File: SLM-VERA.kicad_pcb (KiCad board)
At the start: 2 copper layers, 28.4 x 47.9 mm, 25 parts, among them J1 FH35C-45S-0.3SHW(50), J2 FH35C-45S-0.3SHW(50), U1 FODM217D, U2 FODM217D, U3 FODM217D, U4 ESP32-DevKitC

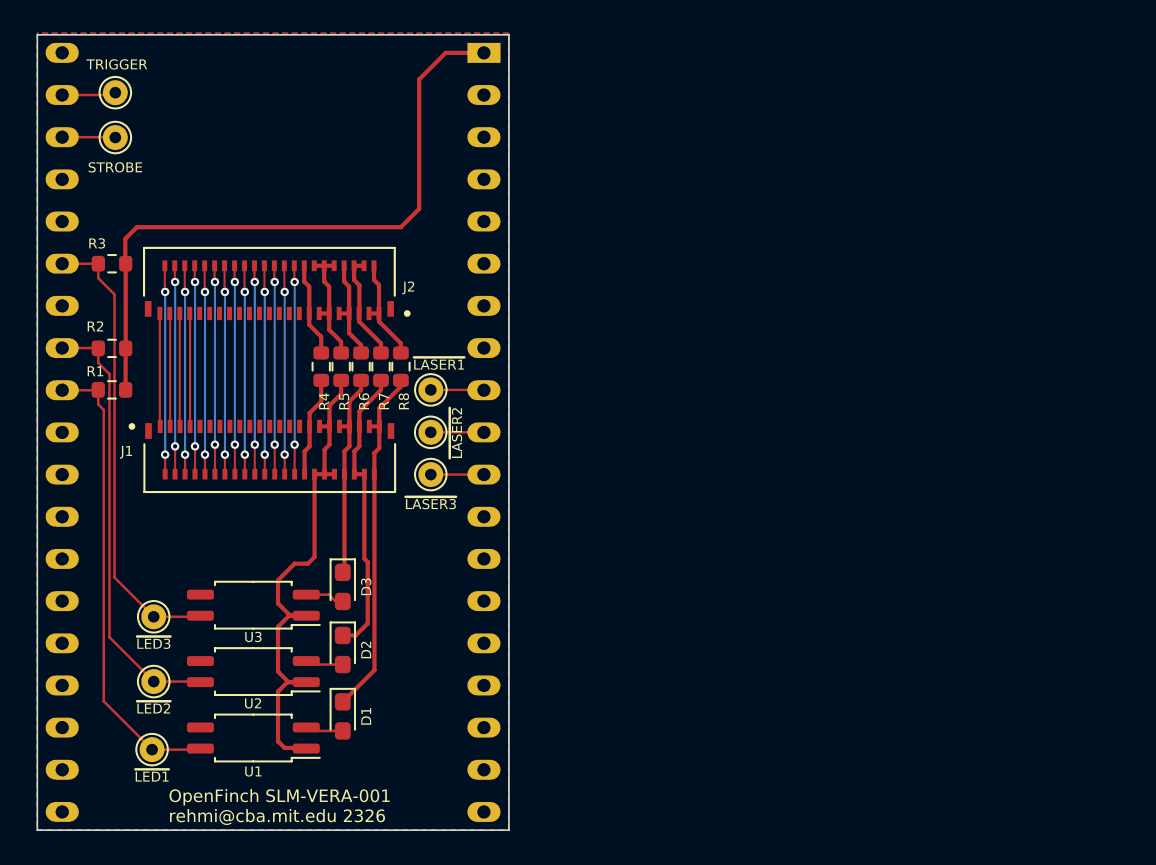
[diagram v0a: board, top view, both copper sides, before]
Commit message: SLM-VERA-002: fixed J1 & J2; all routes on top copper
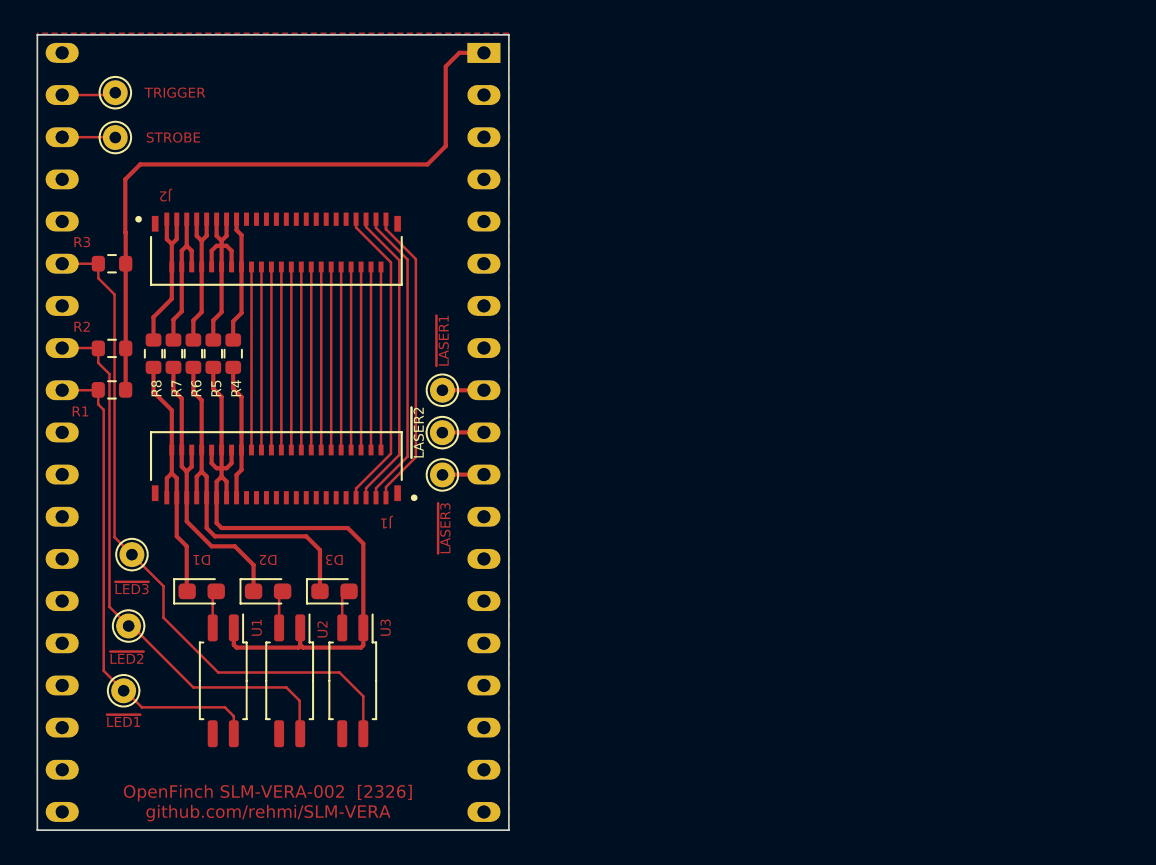
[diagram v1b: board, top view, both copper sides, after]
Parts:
- moved R8 14.9 mm to (107.0, 71.3)
- moved R7 12.5 mm to (108.2, 71.3)
- moved D1 11.4 mm to (109.9, 85.6), turned to 0 degrees
- moved R6 10.1 mm to (109.4, 71.3)
- moved R5 7.74 mm to (110.6, 71.3)
- moved U3 7.52 mm to (119.0, 91.0), turned to -90 degrees
- moved D2 5.72 mm to (113.9, 85.6), turned to 0 degrees
- moved R4 5.36 mm to (111.8, 71.3)
- moved ~{LED3} 3.97 mm to (105.7, 83.4)
- moved ~{LED1} 3.94 mm to (105.2, 91.6)
- moved U1 3.89 mm to (111.2, 91.0), turned to -90 degrees
- moved ~{LED2} 3.67 mm to (105.5, 87.7)
- moved J2 2.91 mm to (114.4, 64.6), turned to 180 degrees
- moved U2 2.26 mm to (115.2, 91.0), turned to -90 degrees
- moved J1 1.55 mm to (114.4, 78.6), turned to 0 degrees
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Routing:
- net /~{LED3}: track 27.6 -> 41.4 mm
- net /IO6: track 6.78 -> 18.5 mm
- net /IO0: track 6.78 -> 18.5 mm
- net /IO4: track 6.78 -> 18.4 mm
- net /IO2: track 6.78 -> 18.3 mm
- net /LED3_IN: track 12.7 -> 21.6 mm
- net /LED+_IN: track 32.5 -> 39.7 mm
- net /~{LED2}: track 26.4 -> 33.5 mm
- net /LED1_IN: track 21.6 -> 15.9 mm
- net /LED+_OUT: track 7.70 -> 12.4 mm
- net /LED1_OUT: track 6.75 -> 9.48 mm
- net /LED3_OUT: track 6.50 -> 9.03 mm
- net /LED2_OUT: track 6.74 -> 9.01 mm
- net /LED-_IN: track 6.29 -> 8.18 mm
- net /LED-_OUT: track 5.90 -> 7.61 mm
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- removed copper zone on B.Cu, net GND
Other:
- board text added: "OpenFinch SLM-VERA-002 [2326] github.com/rehmi/SLM-VERA"
- board text removed: "OpenFinch SLM-VERA-001 rehmi@cba.mit.edu 2326"

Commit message: changed ESP32-Devkit-C to Seeeduino Xiao
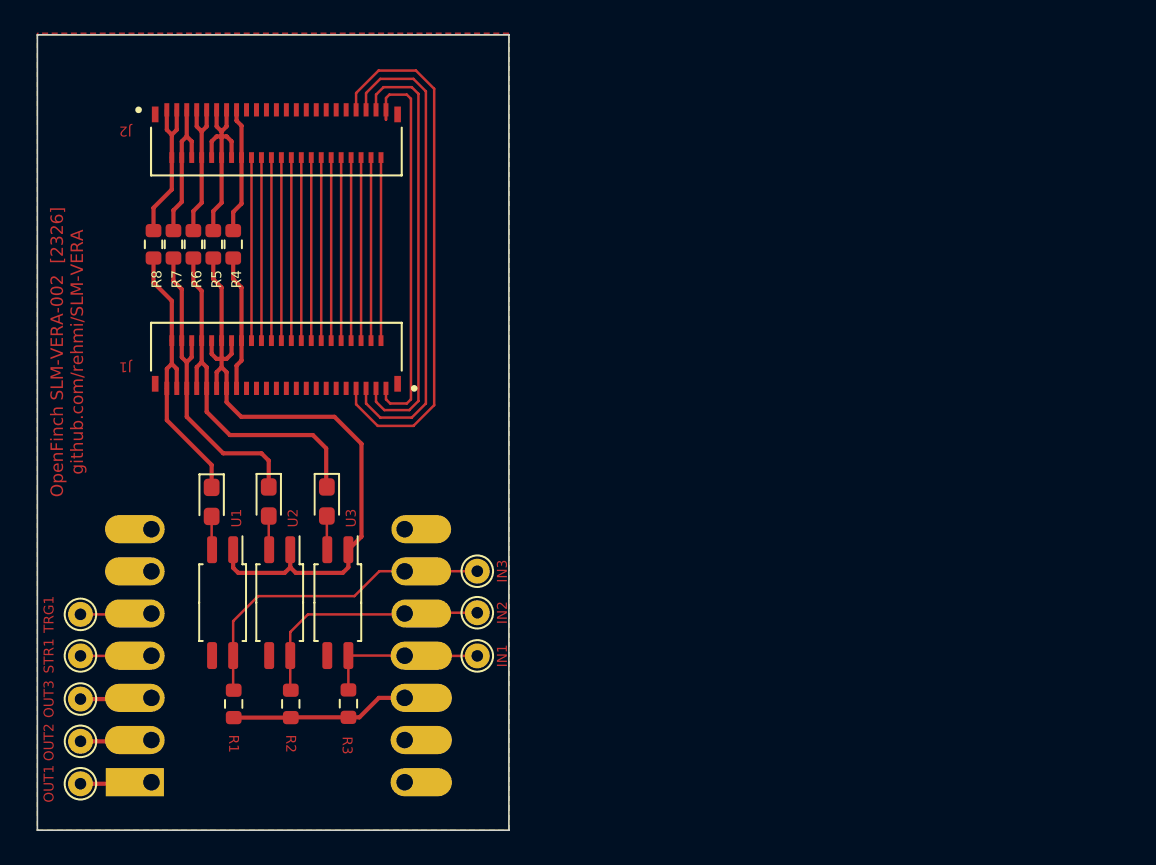
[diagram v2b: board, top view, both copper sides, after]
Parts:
- U4: value ESP32-DevKitC -> Seeed Studio XIAO ESP32S3; footprint PCM_Espressif:ESP32-DevKitC -> Seeed Studio XIAO Series Library:XIAO-Generic-Hybrid-14P-2.54-21X17.8MM
- moved U4 38.4 mm to (114.5, 89.5), turned to 0 degrees
- moved OUT1 32.2 mm to (102.6, 97.2), turned to 180 degrees
- moved TRG1 31.5 mm to (102.6, 87.0)
- moved STR1 31.3 mm to (102.6, 89.5)
- moved R3 30.1 mm to (118.7, 92.4), turned to -90 degrees
- moved OUT2 28.6 mm to (102.6, 94.6), turned to 180 degrees
- moved OUT3 25.6 mm to (102.6, 92.1), turned to 180 degrees
- moved R2 24.0 mm to (115.3, 92.4), turned to -90 degrees
- moved IN3 22.5 mm to (126.5, 84.4)
- moved IN1 21.7 mm to (126.5, 89.5)
- moved IN2 21.0 mm to (126.5, 86.9)
- moved R1 20.3 mm to (111.8, 92.4), turned to -90 degrees
- moved J1 6.59 mm to (114.4, 72.0)
- moved J2 6.59 mm to (114.4, 58.0)
- moved R4 6.59 mm to (111.8, 64.7)
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- renumbered ~{LED3} to IN1, ~{LED2} to IN2, ~{LED1} to IN3, ~{LASER1} to OUT1, ~{LASER2} to OUT2, ~{LASER3} to OUT3, STROBE to STR1, TRIGGER to TRG1
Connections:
- U4 pad 1: +3V3 -> /~{LASER1}
- U4 pad 10: /~{LASER2} -> /~{LED2}
- U4 pad 11: /~{LASER3} -> /~{LED3}
- U4 pad 12: unconnected-(U4-MTMS/GPIO14/ADC2_CH6-Pad12) -> +3V3
- U4 pad 13: unconnected-(U4-MTDI/GPIO12/ADC2_CH5-Pad13) -> GND
- U4 pad 14: GND -> unconnected-(U4-5V-Pad14)
- U4 pad 2: unconnected-(U4-CHIP_PU-Pad2) -> /~{LASER2}
- U4 pad 3: unconnected-(U4-SENSOR_VP/GPIO36/ADC1_CH0-Pad3) -> /~{LASER3}
- U4 pad 4: unconnected-(U4-SENSOR_VN/GPIO39/ADC1_CH3-Pad4) -> /STROBE
- U4 pad 5: unconnected-(U4-VDET_1/GPIO34/ADC1_CH6-Pad5) -> /TRIGGER
- U4 pad 9: /~{LASER1} -> /~{LED1}
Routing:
- net /~{LED3}: track 41.4 -> 9.81 mm
- net +3V3: track 40.0 -> 10.8 mm
- net /~{LED2}: track 33.5 -> 15.1 mm
- net /IO6: track 18.5 -> 32.5 mm
- net /IO4: track 18.4 -> 29.3 mm
- net /~{LED1}: track 29.4 -> 20.1 mm
- net /IO2: track 18.3 -> 26.1 mm
- net /IO0: track 18.5 -> 23.7 mm
- net /~{LASER3}: track 2.53 -> 4.20 mm
- net /~{LASER2}: track 2.53 -> 4.19 mm
- net /~{LASER1}: track 2.52 -> 4.18 mm
- net /LED1_IN: track 15.9 -> 17.1 mm
- net /LED2_IN: track 17.7 -> 18.9 mm
- net /STROBE: track 3.18 -> 4.26 mm
- net /TRIGGER: track 3.16 -> 4.22 mm

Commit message: Redesigned as Raspberry Pi (Zero) hat
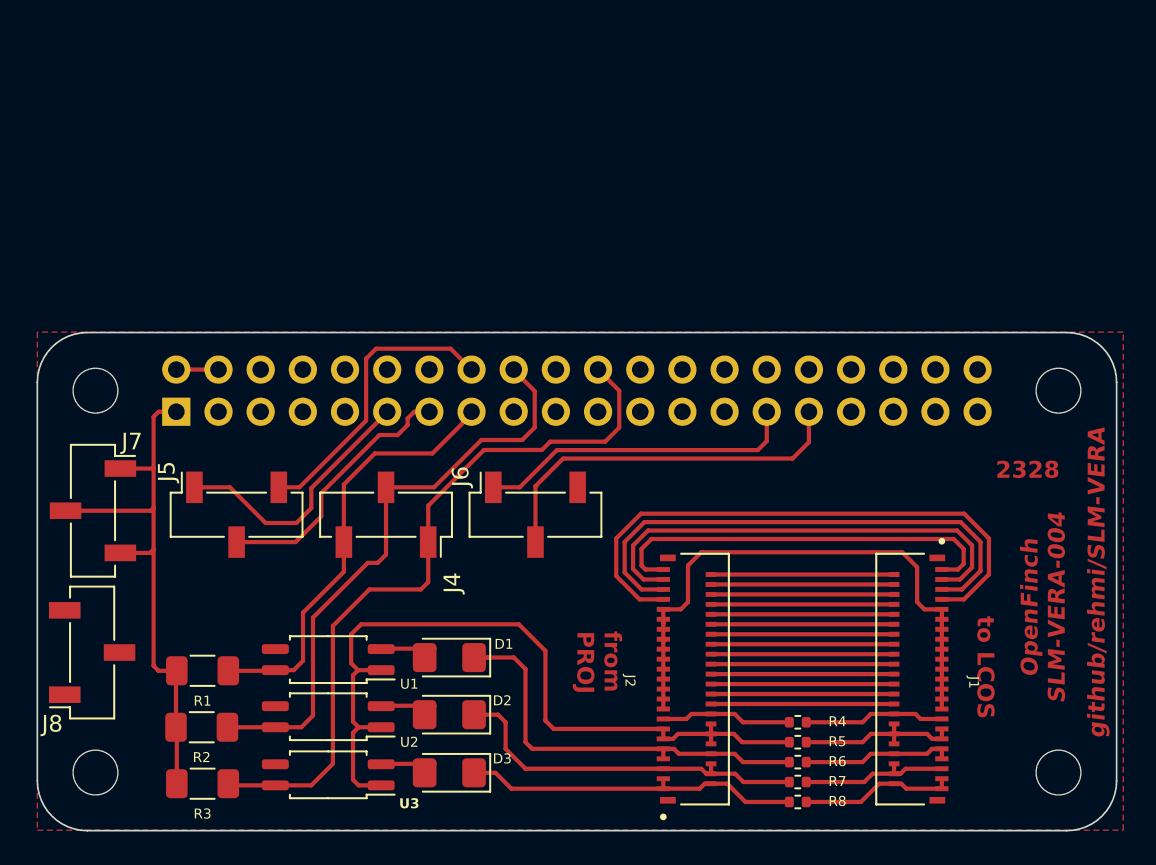
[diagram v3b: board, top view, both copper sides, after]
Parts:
- removed IN1: ~{LI3}, TestPoint:TestPoint_THTPad_D1.5mm_Drill0.7mm
- removed IN2: ~{LI2}, TestPoint:TestPoint_THTPad_D1.5mm_Drill0.7mm
- removed IN3: ~{LI1}, TestPoint:TestPoint_THTPad_D1.5mm_Drill0.7mm
- removed OUT1: ~{LO1}, TestPoint:TestPoint_THTPad_D1.5mm_Drill0.7mm
- removed OUT2: ~{LO2}, TestPoint:TestPoint_THTPad_D1.5mm_Drill0.7mm
- removed OUT3: ~{LO3}, TestPoint:TestPoint_THTPad_D1.5mm_Drill0.7mm
- removed STR1: STR, TestPoint:TestPoint_THTPad_D1.5mm_Drill0.7mm
- removed TRG1: TRG, TestPoint:TestPoint_THTPad_D1.5mm_Drill0.7mm
- removed U4: Seeed Studio XIAO ESP32S3, Seeed Studio XIAO Series Library:XIAO-Generic-Hybrid-14P-2.54-21X17.8MM
- added J3: GPIO, Connector_PinSocket_2.54mm:PinSocket_2x20_P2.54mm_Vertical, B.Cu at (108.4, 74.8)
- added J4: Conn_01x03_Socket, Connector_PinSocket_2.54mm:PinSocket_1x03_P2.54mm_Vertical_SMD_Pin1Right, F.Cu at (121.0, 81.0)
- added J5: Conn_01x03_Socket, Connector_PinSocket_2.54mm:PinSocket_1x03_P2.54mm_Vertical_SMD_Pin1Right, F.Cu at (112.0, 81.0)
- added J6: Conn_01x03_Socket, Connector_PinSocket_2.54mm:PinSocket_1x03_P2.54mm_Vertical_SMD_Pin1Right, F.Cu at (130.0, 81.0)
- added J7: Conn_01x03_Socket, Connector_PinSocket_2.54mm:PinSocket_1x03_P2.54mm_Vertical_SMD_Pin1Right, F.Cu at (103.3, 80.8)
- added J8: Conn_01x03_Socket, Connector_PinSocket_2.54mm:PinSocket_1x03_P2.54mm_Vertical_SMD_Pin1Right, F.Cu at (103.3, 89.3)
- added MH1: MountingHole_2.7mm_M2.5, MountingHole:MountingHole_2.7mm_M2.5, F.Cu at (103.5, 73.5)
- added MH2: MountingHole_2.7mm_M2.5, MountingHole:MountingHole_2.7mm_M2.5, F.Cu at (161.5, 73.5)
- added MH3: MountingHole_2.7mm_M2.5, MountingHole:MountingHole_2.7mm_M2.5, F.Cu at (103.5, 96.5)
- added MH4: MountingHole_2.7mm_M2.5, MountingHole:MountingHole_2.7mm_M2.5, F.Cu at (161.5, 96.5)
- D1, D2, D3: footprint LED_SMD:LED_0603_1608Metric_Pad1.05x0.95mm_HandSolder -> LED_SMD:LED_1206_3216Metric_Pad1.42x1.75mm_HandSolder
- R1, R2, R3: footprint Resistor_SMD:R_0603_1608Metric -> Resistor_SMD:R_1206_3216Metric_Pad1.30x1.75mm_HandSolder
- R4, R5, R6, R7, R8: footprint Resistor_SMD:R_0603_1608Metric -> Resistor_SMD:R_0402_1005Metric
- moved R8 51.3 mm to (145.8, 98.3), turned to 180 degrees
- moved R7 49.6 mm to (145.8, 97.1), turned to 180 degrees
- moved R6 47.9 mm to (145.8, 95.9), turned to 180 degrees
- moved R5 46.2 mm to (145.8, 94.7), turned to 180 degrees
- moved R4 44.6 mm to (145.8, 93.5), turned to 180 degrees
- moved J1 43.1 mm to (153.1, 90.9), turned to 90 degrees
- moved J2 41.1 mm to (139.1, 90.9), turned to -90 degrees
- moved D3 17.9 mm to (124.8, 96.5), turned to 180 degrees
- moved D1 17.1 mm to (124.8, 89.6), turned to 180 degrees
- moved D2 16.8 mm to (124.8, 93.0), turned to 180 degrees
- moved U3 10.4 mm to (117.5, 96.7), turned to 180 degrees
- moved R3 10.0 mm to (110.0, 97.2), turned to 180 degrees
- moved U2 7.47 mm to (117.5, 93.2), turned to 180 degrees
- moved U1 7.23 mm to (117.5, 89.7), turned to 180 degrees
- moved R2 5.54 mm to (109.9, 93.8), turned to 180 degrees
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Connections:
- net /~{LED1} renamed /GPIO22
- net /~{LED2} renamed /GPIO24
- net /~{LED3} renamed /GPIO25
- D1 pad 1: /LED1_IN -> /LED3_IN
- D3 pad 1: /LED3_IN -> /LED1_IN
- J1 pad 30: /LED-_IN -> /LED-_OUT
- J1 pad 31: /LED-_IN -> /LED-_OUT
- J1 pad 32: /LED+_IN -> /LED+_OUT
- J1 pad 33: /LED+_IN -> /LED+_OUT
- J1 pad 34: /LED+_IN -> /LED+_OUT
- J1 pad 35: /LED+_IN -> /LED+_OUT
- J1 pad 36: /LED+_IN -> /LED+_OUT
- J1 pad 37: /LED3_IN -> /LED3_OUT
- J1 pad 38: /LED3_IN -> /LED3_OUT
- J1 pad 39: /LED3_IN -> /LED3_OUT
- J1 pad 40: /LED2_IN -> /LED2_OUT
- J1 pad 41: /LED2_IN -> /LED2_OUT
- J1 pad 42: /LED2_IN -> /LED2_OUT
- J1 pad 43: /LED1_IN -> /LED1_OUT
- J1 pad 44: /LED1_IN -> /LED1_OUT
- J1 pad 45: /LED1_IN -> /LED1_OUT
- J2 pad 1: /LED1_OUT -> /LED1_IN
- J2 pad 10: /LED+_OUT -> /LED+_IN
- J2 pad 11: /LED+_OUT -> /LED+_IN
- J2 pad 12: /LED+_OUT -> /LED+_IN
- J2 pad 13: /LED+_OUT -> /LED+_IN
- J2 pad 14: /LED+_OUT -> /LED+_IN
- J2 pad 15: /LED-_OUT -> /LED-_IN
- J2 pad 16: /LED-_OUT -> /LED-_IN
- J2 pad 2: /LED1_OUT -> /LED1_IN
- J2 pad 3: /LED1_OUT -> /LED1_IN
- J2 pad 4: /LED2_OUT -> /LED2_IN
- J2 pad 5: /LED2_OUT -> /LED2_IN
- J2 pad 6: /LED2_OUT -> /LED2_IN
- J2 pad 7: /LED3_OUT -> /LED3_IN
- J2 pad 8: /LED3_OUT -> /LED3_IN
- J2 pad 9: /LED3_OUT -> /LED3_IN
- R4 pad 1: /LED-_IN -> /LED-_OUT
- R4 pad 2: /LED-_OUT -> /LED-_IN
- R5 pad 1: /LED+_IN -> /LED+_OUT
- R5 pad 2: /LED+_OUT -> /LED+_IN
- R6 pad 1: /LED3_IN -> /LED3_OUT
- R6 pad 2: /LED3_OUT -> /LED3_IN
- R7 pad 1: /LED2_IN -> /LED2_OUT
- R7 pad 2: /LED2_OUT -> /LED2_IN
- R8 pad 1: /LED1_IN -> /LED1_OUT
- R8 pad 2: /LED1_OUT -> /LED1_IN
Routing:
- net GND: track 0.00 -> 34.6 mm
- net /GPIO25: track 9.81 -> 44.0 mm
- net +3V3: track 10.8 -> 33.8 mm
- net /GPIO6: track 0.00 -> 22.8 mm
- net /GPIO24: track 15.1 -> 35.8 mm
- net /GPIO5: track 0.00 -> 19.4 mm
- net /GPIO23: track 0.00 -> 17.8 mm
- net /GPIO17: track 0.00 -> 16.0 mm
- net /GPIO27: track 0.00 -> 15.9 mm
- net /LED+_IN: track 40.0 -> 47.5 mm
- net /GPIO22: track 20.1 -> 25.8 mm
- net /STROBE: track 4.26 -> 0.00 mm
- net /TRIGGER: track 4.22 -> 0.00 mm
- net /~{LASER3}: track 4.20 -> 0.00 mm
- net /~{LASER2}: track 4.19 -> 0.00 mm
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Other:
- board size 28.4 x 47.9 mm -> 65 x 30 mm
- board text added: "2328"
- board text added: "OpenFinch SLM-VERA-004"
- board text added: "from PROJ"
- board text added: "github/rehmi/SLM-VERA"
- board text added: "locked"
- board text added: "to LCOS"
- board text removed: "OpenFinch SLM-VERA-002 [2326] github.com/rehmi/SLM-VERA"

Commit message: updated R1-R3 values to 1k on SLM-VERA-004
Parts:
- R1, R2, R3: value 10k -> 1k
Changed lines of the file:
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@@
         (effects (font (size 0.6 0.6) (thickness 0.15)))
     )
-    (fp_text value "10k" (at 0 1.82) (layer "F.Fab")
+    (fp_text value "1k" (at 0 1.82) (layer "F.Fab")
         (effects (font (size 1 1) (thickness 0.15)))
     )
@@
         (effects (font (size 0.6 0.6) (thickness 0.15)))
     )
-    (fp_text value "10k" (at 0 1.82) (layer "F.Fab")
+    (fp_text value "1k" (at 0 1.82) (layer "F.Fab")
         (effects (font (size 1 1) (thickness 0.15)))
     )
@@
         (effects (font (size 0.6 0.6) (thickness 0.15)))
     )
-    (fp_text value "10k" (at 0 1.82) (layer "F.Fab")
-        (effects (font (size 1 1) (thickness 0.15)))
-    )
+    (fp_text value "1k" (at 0 1.82) (layer "F.Fab")
+        (effects (font (size 1 1) (thickness 0.15)))
+    )
